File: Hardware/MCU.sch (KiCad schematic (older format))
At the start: 24 parts, among them J2 LCD4x20, U10 74HC14, U11 74HC14, U9 BluePill_STM32F103C

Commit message: Add files via upload
HW layout and libs
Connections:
- wire segments 63 -> 54
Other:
- note added: "int motor2_input1 = PA8;\nint motor2_input2 = PA10;\nint motor1_input1 = PB8;\nint motor1_input2 = PB9;\n\nint step_M1 = PB10;\nint cmd_M1 = PB11;\nint step_M2 = PA11;\nint cmd_M2 = PA12;\n\nconst int limitUpper_M1 = PB0;\nconst int limitLower_M1= PB1;\nconst int limitUpper_M2 = PB12;\nconst int limitLower_M2 = PB13;\n\nconst int out_M1 = PB15;\nconst int out_M2 = PB14;\n\nint motor2_Enc_A = PA3;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"
- moved on the sheet: 1U3, 1U4, 1U5, R16, R17, U10A, U10B, U10C, U10D, U10F, U9

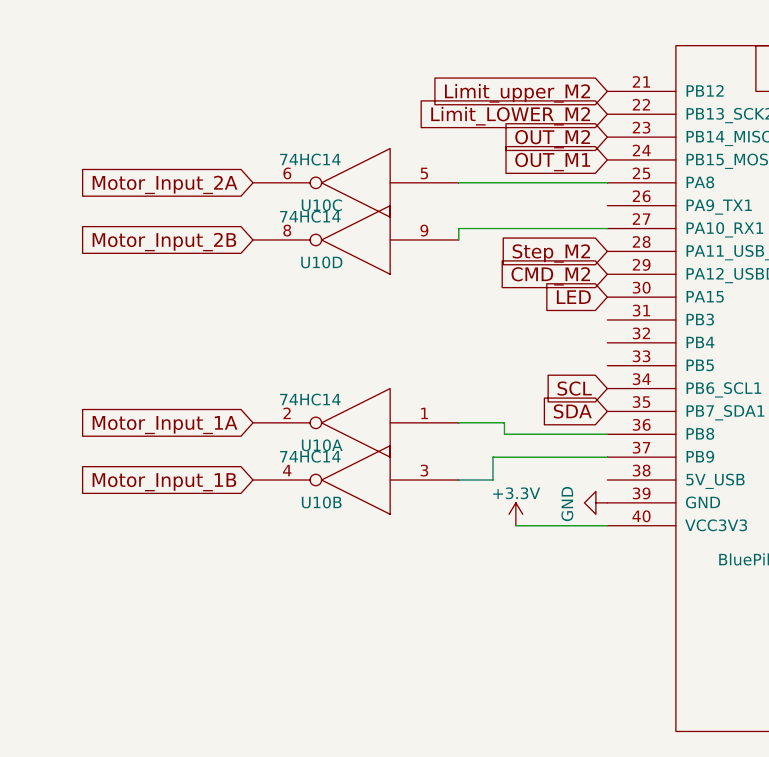
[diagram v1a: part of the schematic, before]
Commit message: Layout - some pin changes to 74hc14
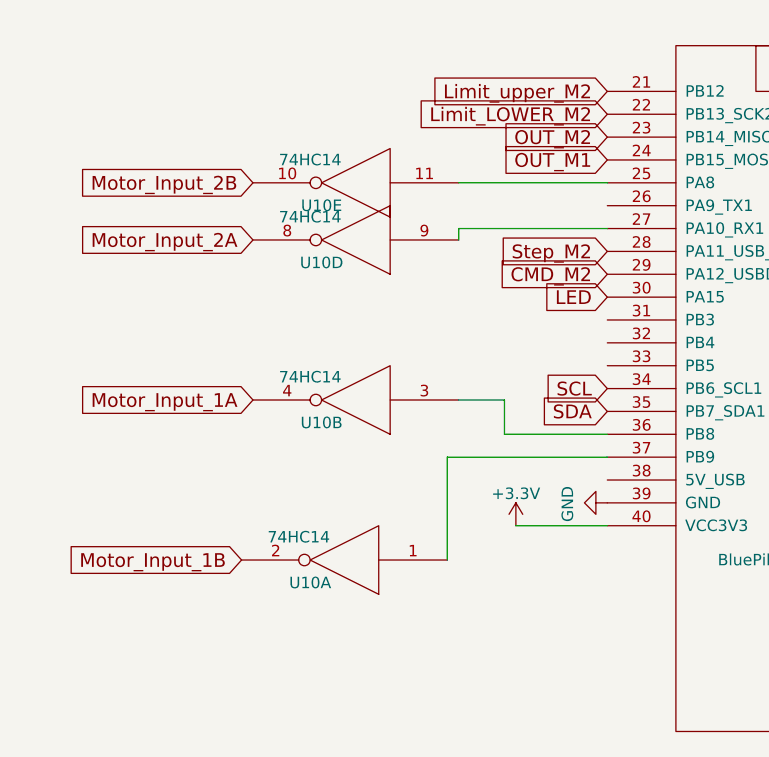
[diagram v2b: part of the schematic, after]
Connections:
- wire segments 54 -> 53
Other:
- moved on the sheet: U10A, U10B
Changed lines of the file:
@@
 Text GLabel 2800 2300 0    60   Input ~ 0
 SCL
-Text GLabel 1250 2450 0    60   Input ~ 0
+Text GLabel 1250 2350 0    60   Input ~ 0
 Motor_Input_1A
-Text GLabel 1250 2700 0    60   Input ~ 0
+Text GLabel 1200 3050 0    60   Input ~ 0
 Motor_Input_1B
+Text GLabel 1250 1650 0    60   Input ~ 0
+Motor_Input_2A
 Text GLabel 1250 1400 0    60   Input ~ 0
-Motor_Input_2A
-Text GLabel 1250 1650 0    60   Input ~ 0
 Motor_Input_2B
 Text GLabel 4550 1600 2    60   Input ~ 0
@@
 L 74HC14 U10
 U 1 1 5A67D171
-P 1700 2450
-F 0 "U10" H 1850 2550 50  0000 C CNN
-F 1 "74HC14" H 1900 2350 50  0000 C CNN
-F 2 "Housings_SOIC:SOIC-14_3.9x8.7mm_Pitch1.27mm" H 1700 2450 50  0001 C CNN
-F 3 "" H 1700 2450 50  0001 C CNN
-	1    1700 2450
+P 1650 3050
+F 0 "U10" H 1800 3150 50  0000 C CNN
+F 1 "74HC14" H 1850 2950 50  0000 C CNN
+F 2 "Housings_SOIC:SOIC-14_3.9x8.7mm_Pitch1.27mm" H 1650 3050 50  0001 C CNN
+F 3 "" H 1650 3050 50  0001 C CNN
+	1    1650 3050
 	-1   0    0    1
 $EndComp
@@
 L 74HC14 U10
 U 2 1 5A67D1B2
-P 1700 2700
-F 0 "U10" H 1850 2800 50  0000 C CNN
-F 1 "74HC14" H 1900 2600 50  0000 C CNN
-F 2 "Housings_SOIC:SOIC-14_3.9x8.7mm_Pitch1.27mm" H 1700 2700 50  0001 C CNN
-F 3 "" H 1700 2700 50  0001 C CNN
-	2    1700 2700
+P 1700 2350
+F 0 "U10" H 1850 2450 50  0000 C CNN
+F 1 "74HC14" H 1900 2250 50  0000 C CNN
+F 2 "Housings_SOIC:SOIC-14_3.9x8.7mm_Pitch1.27mm" H 1700 2350 50  0001 C CNN
+F 3 "" H 1700 2350 50  0001 C CNN
+	2    1700 2350
 	-1   0    0    1
 $EndComp
 $Comp
 L 74HC14 U10
-U 3 1 5A67D1FD
+U 5 1 5A67D1FD
 P 1700 1400
 F 0 "U10" H 1850 1500 50  0000 C CNN
@@
 F 2 "Housings_SOIC:SOIC-14_3.9x8.7mm_Pitch1.27mm" H 1700 1400 50  0001 C CNN
 F 3 "" H 1700 1400 50  0001 C CNN
-	3    1700 1400
+	5    1700 1400
 	-1   0    0    1
 $EndComp
@@
 	2150 1600 2150 1650
 Wire Wire Line
-	2800 2500 2350 2500
-Wire Wire Line
-	2350 2500 2350 2450
-Wire Wire Line
-	2350 2450 2150 2450
-Wire Wire Line
-	2800 2600 2300 2600
-Wire Wire Line
-	2300 2600 2300 2700
-Wire Wire Line
-	2300 2700 2150 2700
+	2350 2500 2800 2500
+Wire Wire Line
+	2350 2350 2350 2500
+Wire Wire Line
+	2100 2600 2800 2600
 $Comp
 L VDD #PWR056
@@
 Text GLabel 2800 1900 0    60   Input ~ 0
 LED
+Wire Wire Line
+	2150 2350 2350 2350
+Wire Wire Line
+	2100 3050 2100 2600
 $EndSCHEMATC

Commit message: Add files via upload
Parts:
- removed 1U6, 1U7: 0,1U, Capacitors_SMD:C_0805_HandSoldering, symbol C
- removed C6, C7, C8: 0.1uF, Capacitors_SMD:C_0805_HandSoldering, symbol C
- removed D10, D11, D12: 1m4148, Diodes_SMD:D_MiniMELF_Handsoldering, symbol D
- removed R18, R19, R20, R21, R22, R23: 10K, Resistors_SMD:R_0805_HandSoldering, symbol R
- removed ROT1: ROTARY-ENCODER, Libs:ROTARY-ENCODER-Ebay, symbol ROTARY-ENCODER-Ebay
- removed U11: 74HC14, Housings_SOIC:SOIC-14_3.9x8.7mm_Pitch1.27mm, symbol 74HC14
- added J?: RotEnc, Pin_Headers:Pin_Header_Straight_1x04_Pitch2.54mm, symbol Conn_01x04
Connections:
- wire segments 53 -> 22
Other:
- note removed: "Menu encoder and display"
- moved on the sheet: J2

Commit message: Add files via upload
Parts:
- removed J2: LCD4x20, Pin_Headers:Pin_Header_Straight_1x04_Pitch2.54mm, symbol Conn_01x04
- removed J?: RotEnc, Pin_Headers:Pin_Header_Straight_1x04_Pitch2.54mm, symbol Conn_01x04
- added J2: LCD_and_RotEnc, Pin_Headers:Pin_Header_Straight_1x07_Pitch2.54mm, symbol Conn_01x07
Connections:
- wire segments 22 -> 24
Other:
- moved on the sheet: 1U5
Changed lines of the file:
@@
 LIBS:L298N
 LIBS:WS2812B
+LIBS:a4973
 LIBS:a3968
 LIBS:lm2675
@@
 L C 1U5
 U 1 1 5A674C9E
-P 9350 1000
-F 0 "1U5" H 9465 1046 50  0000 L CNN
-F 1 "0,1U" H 9465 955 50  0000 L CNN
-F 2 "Capacitors_SMD:C_0805_HandSoldering" H 9388 850 50  0001 C CNN
-F 3 "" H 9350 1000 50  0001 C CNN
-	1    9350 1000
+P 9250 1050
+F 0 "1U5" H 9365 1096 50  0000 L CNN
+F 1 "0,1U" H 9365 1005 50  0000 L CNN
+F 2 "Capacitors_SMD:C_0805_HandSoldering" H 9288 900 50  0001 C CNN
+F 3 "" H 9250 1050 50  0001 C CNN
+	1    9250 1050
 	1    0    0    -1
 $EndComp
@@
 L GND #PWR031
 U 1 1 5A674CAB
-P 9350 1150
-F 0 "#PWR031" H 9350 900 50  0001 C CNN
-F 1 "GND" H 9355 977 50  0000 C CNN
-F 2 "" H 9350 1150 50  0001 C CNN
-F 3 "" H 9350 1150 50  0001 C CNN
-	1    9350 1150
+P 9250 1200
+F 0 "#PWR031" H 9250 950 50  0001 C CNN
+F 1 "GND" H 9255 1027 50  0000 C CNN
+F 2 "" H 9250 1200 50  0001 C CNN
+F 3 "" H 9250 1200 50  0001 C CNN
+	1    9250 1200
 	1    0    0    -1
 $EndComp
@@
 Text GLabel 2800 1800 0    60   Input ~ 0
 CMD_M2
-Text GLabel 4550 2000 2    60   Input ~ 0
-LED
 $Comp
 L C 1U4
@@
 	10700 1550 10700 1300
 $Comp
-L Conn_01x04 J2
-U 1 1 5A70741F
-P 7250 1350
-F 0 "J2" H 7250 1550 50  0000 C CNN
-F 1 "LCD4x20" V 7400 1300 50  0000 C CNN
-F 2 "Pin_Headers:Pin_Header_Straight_1x04_Pitch2.54mm" H 7250 1350 50  0001 C CNN
-F 3 "" H 7250 1350 50  0001 C CNN
-	1    7250 1350
-	1    0    0    -1
-$EndComp
-$Comp
-L VCC #PWR039
+L VCC #PWR036
 U 1 1 5A707439
-P 7050 1250
-F 0 "#PWR039" H 7050 1100 50  0001 C CNN
-F 1 "VCC" H 7067 1423 50  0000 C CNN
-F 2 "" H 7050 1250 50  0001 C CNN
-F 3 "" H 7050 1250 50  0001 C CNN
-	1    7050 1250
-	1    0    0    -1
-$EndComp
-$Comp
-L GND #PWR040
+P 6700 1050
+F 0 "#PWR036" H 6700 900 50  0001 C CNN
+F 1 "VCC" H 6717 1223 50  0000 C CNN
+F 2 "" H 6700 1050 50  0001 C CNN
+F 3 "" H 6700 1050 50  0001 C CNN
+	1    6700 1050
+	1    0    0    -1
+$EndComp
+$Comp
+L GND #PWR037
 U 1 1 5A70743F
-P 7050 1550
-F 0 "#PWR040" H 7050 1300 50  0001 C CNN
-F 1 "GND" H 7055 1377 50  0000 C CNN
-F 2 "" H 7050 1550 50  0001 C CNN
-F 3 "" H 7050 1550 50  0001 C CNN
-	1    7050 1550
-	1    0    0    -1
-$EndComp
-Text GLabel 7050 1350 0    60   Input ~ 0
+P 6700 1750
+F 0 "#PWR037" H 6700 1500 50  0001 C CNN
+F 1 "GND" H 6705 1577 50  0000 C CNN
+F 2 "" H 6700 1750 50  0001 C CNN
+F 3 "" H 6700 1750 50  0001 C CNN
+	1    6700 1750
+	1    0    0    -1
+$EndComp
+Text GLabel 6700 1300 0    60   Input ~ 0
 SCL
-Text GLabel 7050 1450 0    60   Input ~ 0
+Text GLabel 6700 1200 0    60   Input ~ 0
 SDA
 Wire Wire Line
@@
 	2800 2900 2400 2900
 $Comp
-L +3.3V #PWR046
+L +3.3V #PWR038
 U 1 1 5A7153CF
 P 2400 2900
-F 0 "#PWR046" H 2400 2750 50  0001 C CNN
+F 0 "#PWR038" H 2400 2750 50  0001 C CNN
 F 1 "+3.3V" H 2400 3040 50  0000 C CNN
 F 2 "" H 2400 2900 50  0001 C CNN
@@
 $EndComp
 $Comp
-L +3.3V #PWR047
+L +3.3V #PWR039
 U 1 1 5A715491
 P 8850 900
-F 0 "#PWR047" H 8850 750 50  0001 C CNN
+F 0 "#PWR039" H 8850 750 50  0001 C CNN
 F 1 "+3.3V" H 8850 1040 50  0000 C CNN
 F 2 "" H 8850 900 50  0001 C CNN
@@
 $EndComp
 $Comp
-L +3.3V #PWR048
+L +3.3V #PWR040
 U 1 1 5A7154F3
 P 8550 900
-F 0 "#PWR048" H 8550 750 50  0001 C CNN
+F 0 "#PWR040" H 8550 750 50  0001 C CNN
 F 1 "+3.3V" H 8550 1040 50  0000 C CNN
 F 2 "" H 8550 900 50  0001 C CNN
@@
 $EndComp
 $Comp
-L +3.3V #PWR049
+L +3.3V #PWR041
 U 1 1 5A715555
-P 9350 850
-F 0 "#PWR049" H 9350 700 50  0001 C CNN
-F 1 "+3.3V" H 9350 990 50  0000 C CNN
-F 2 "" H 9350 850 50  0001 C CNN
-F 3 "" H 9350 850 50  0001 C CNN
-	1    9350 850
-	1    0    0    -1
-$EndComp
-$Comp
-L +3.3V #PWR050
+P 9250 900
+F 0 "#PWR041" H 9250 750 50  0001 C CNN
+F 1 "+3.3V" H 9250 1040 50  0000 C CNN
+F 2 "" H 9250 900 50  0001 C CNN
+F 3 "" H 9250 900 50  0001 C CNN
+	1    9250 900
+	1    0    0    -1
+$EndComp
+$Comp
+L +3.3V #PWR042
 U 1 1 5A71590E
 P 5100 1050
-F 0 "#PWR050" H 5100 900 50  0001 C CNN
+F 0 "#PWR042" H 5100 900 50  0001 C CNN
 F 1 "+3.3V" H 5100 1190 50  0000 C CNN
 F 2 "" H 5100 1050 50  0001 C CNN
@@
 	10500 2400 10500 2500
 $Comp
-L GND #PWR051
+L GND #PWR043
 U 1 1 5A7162E9
 P 10500 2750
-F 0 "#PWR051" H 10500 2500 50  0001 C CNN
+F 0 "#PWR043" H 10500 2500 50  0001 C CNN
 F 1 "GND" H 10505 2577 50  0000 C CNN
 F 2 "" H 10500 2750 50  0001 C CNN
@@
 	2100 2600 2800 2600
 $Comp
-L VDD #PWR056
+L VDD #PWR044
 U 1 1 5A7C31A2
 P 10500 2300
-F 0 "#PWR056" H 10500 2150 50  0001 C CNN
+F 0 "#PWR044" H 10500 2150 50  0001 C CNN
 F 1 "+5V" H 10500 2450 50  0000 C CNN
 F 2 "" H 10500 2300 50  0001 C CNN
@@
 Wire Wire Line
 	2100 3050 2100 2600
-$Comp
-L Conn_01x04 J?
-U 1 1 5A836054
-P 7250 2000
-F 0 "J?" H 7250 2200 50  0000 C CNN
-F 1 "RotEnc" V 7400 1950 50  0000 C CNN
-F 2 "Pin_Headers:Pin_Header_Straight_1x04_Pitch2.54mm" H 7250 2000 50  0001 C CNN
-F 3 "" H 7250 2000 50  0001 C CNN
-	1    7250 2000
-	1    0    0    -1
-$EndComp
-Text GLabel 7050 2000 0    60   Input ~ 0
+Text GLabel 6700 1500 0    60   Input ~ 0
 Rot_Enc_A
-Text GLabel 7050 2100 0    60   Input ~ 0
+Text GLabel 6700 1600 0    60   Input ~ 0
 Rot_Enc_B
-Text GLabel 7050 1900 0    60   Input ~ 0
+Text GLabel 6700 1400 0    60   Input ~ 0
 Rot_Enc_SW
+$Comp
+L Conn_01x07 J2
+U 1 1 5A8AB16A
+P 6900 1400
+F 0 "J2" H 6900 1800 50  0000 C CNN
+F 1 "LCD_and_RotEnc" V 7050 1400 50  0000 C CNN
+F 2 "Pin_Headers:Pin_Header_Straight_1x07_Pitch2.54mm" H 6900 1400 50  0001 C CNN
+F 3 "" H 6900 1400 50  0001 C CNN
+	1    6900 1400
+	1    0    0    -1
+$EndComp
+Wire Wire Line
+	6700 1750 6700 1700
+Wire Wire Line
+	6700 1050 6700 1100
 $EndSCHEMATC
